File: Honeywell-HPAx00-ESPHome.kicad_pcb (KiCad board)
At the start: 2 copper layers, 215.9 x 50.8 mm, 25 parts, among them J1 Conn_01x06, J2 Conn_01x01, J3 Conn_01x01, J4 Conn_01x01, J5 Conn_01x01, J6 Conn_01x01, J7 Conn_01x01, U1 mini_esp32

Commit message: Update design
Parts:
- moved C1 47.9 mm to (187.0, 102.7)
- moved C2 47.9 mm to (152.0, 101.0)
- moved C3 47.9 mm to (108.4, 80.7)
- moved C4 47.9 mm to (142.2, 106.2)
- moved C5 47.9 mm to (65.2, 88.2)
- moved C6 47.9 mm to (203.7, 83.7)
- moved D1 47.9 mm to (145.2, 103.7)
- moved D10 47.9 mm to (199.2, 78.7)
- moved D11 47.9 mm to (229.7, 88.7)
- moved D2 47.9 mm to (137.5, 105.6)
- moved D3 47.9 mm to (90.2, 80.7)
- moved D4 47.9 mm to (90.2, 96.2)
- moved D5 47.9 mm to (59.7, 98.7)
- moved D7 47.9 mm to (59.7, 78.7)
- moved D8 47.9 mm to (199.2, 98.7)
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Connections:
- U1 pad 13: unconnected-(U1-IO_14/TMS-Pad13) -> BUTT_PREFILTER
- U1 pad 26: /FAN_W -> /FAN_L
- U1 pad 27: /FAN_H -> /FAN_W
- U1 pad 28: /FAN_L -> BUTT_FILTER
- U1 pad 29: unconnected-(U1-IO_17/D3-Pad29) -> /FAN_H
- U1 pad 30: unconnected-(U1-IO_12/TDI-Pad30) -> BUTT_TIMER
- U1 pad 32: BUTT_TIMER -> unconnected-(U1-IO_04-Pad32)
- U1 pad 34: BUTT_PREFILTER -> unconnected-(U1-IO_00-Pad34)
- U1 pad 36: BUTT_FILTER -> Net-(D2-DIN)
- U1 pad 6: Net-(D2-DIN) -> unconnected-(U1-IO_26/D0-Pad6)
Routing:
- net Net-(D2-DIN): track 58.9 -> 25.2 mm
- net BUTT_PREFILTER: track 87.2 -> 114.1 mm, vias 2 -> 0
- net BUTT_TIMER: track 126.9 -> 142.8 mm, vias 4 -> 0
- net Net-(D2-DOUT): track 72.6 -> 86.5 mm, vias 0 -> 2
- net /FAN_H: track 74.6 -> 82.6 mm
- net /FAN_W: track 58.9 -> 63.8 mm, vias 1 -> 2
- net BUTT_FILTER: track 101.0 -> 97.2 mm, vias 2 -> 0
- net Net-(D4-DOUT): track 44.2 -> 40.4 mm, vias 0 -> 2
- net /FAN_M: track 67.3 -> 69.1 mm
- net GND: track 170.3 -> 168.5 mm
- net Net-(D7-DOUT): track 187.5 -> 189.0 mm, vias 2 -> 4
- net BUTT_DIMMER: track 73.8 -> 74.3 mm, vias 2 -> 0
- net /FAN_L: track 63.1 -> 62.8 mm, vias 2 -> 1
- net +5V: track 284.3 -> 284.1 mm, vias 5 -> 7
- net BUTT_TURBO: track 42.5 -> 42.6 mm, vias 2 -> 0

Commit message: final tweaks
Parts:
- J2, J3, J4, J5, J6, J7: footprint TestPoint:TestPoint_THTPad_D1.5mm_Drill0.7mm -> TestPoint:TestPoint_THTPad_D2.0mm_Drill1.0mm

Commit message: Fix issues from production
1. clear space around buttons on ground plane
2. increase capacitor to 4.7mF (1mF would be an absolute minimum)
3. increase hole size for connector, since it's a very tight fit
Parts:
- C3: value 470u -> 4700u; footprint Capacitor_THT:CP_Radial_D8.0mm_P3.50mm -> Capacitor_THT:CP_Radial_D12.5mm_P5.00mm
- moved C3 2.42 mm to (110.0, 82.5)
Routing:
- net GND: track 168.5 -> 173.0 mm
- net +5V: track 284.1 -> 284.6 mm

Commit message: Update with complete instructions
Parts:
- C3: value 4700u -> 1000uF; footprint Capacitor_THT:CP_Radial_D12.5mm_P5.00mm -> Capacitor_THT:CP_Radial_D8.0mm_P3.50mm
- moved C3 4.16 mm to (106.0, 81.3), turned to -90 degrees
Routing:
- net GND: track 173.0 -> 95.9 mm
- net BUTT_FILTER: track 97.2 -> 107.8 mm
- net +5V: track 284.6 -> 285.5 mm

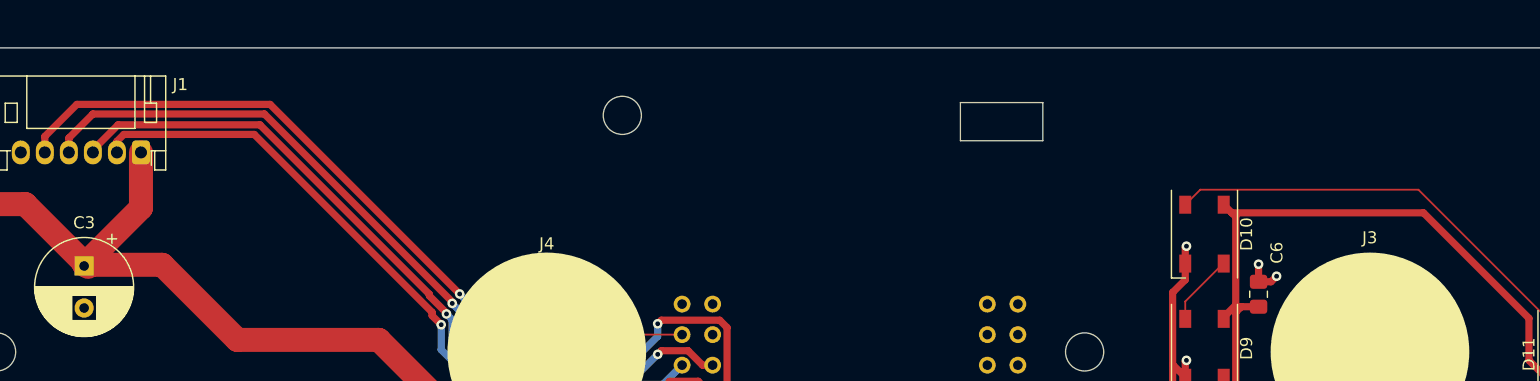
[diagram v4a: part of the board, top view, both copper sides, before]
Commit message: Add connector for extra 5V PSU
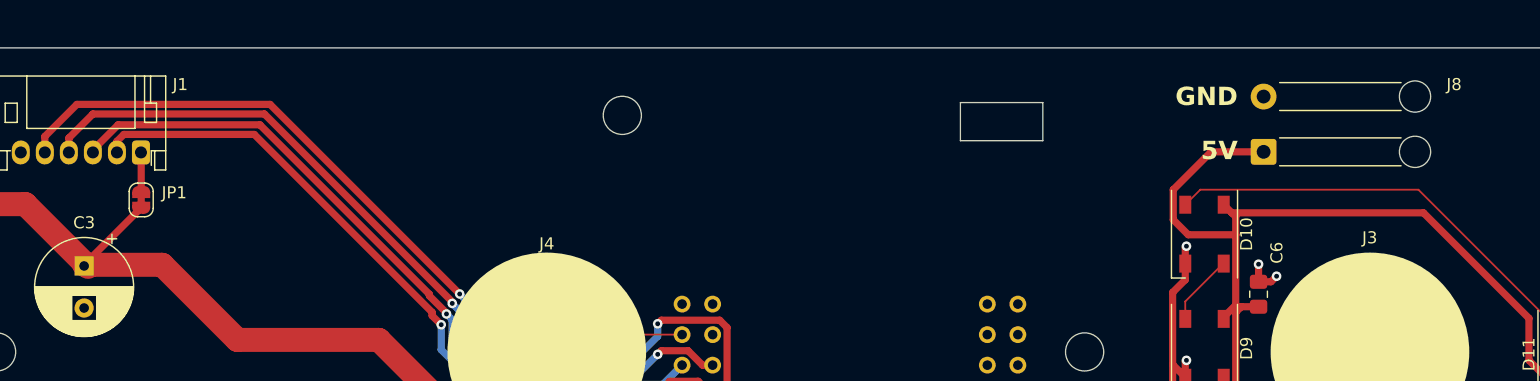
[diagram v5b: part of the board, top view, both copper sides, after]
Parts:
- added J8: Conn_01x02, Connector_Wire:SolderWire-0.5sqmm_1x02_P4.6mm_D0.9mm_OD2.1mm_Relief, F.Cu at (204.2, 71.8)
- added JP1: Jumper_2_Bridged, Jumper:SolderJumper-2_P1.3mm_Bridged_RoundedPad1.0x1.5mm, F.Cu at (110.8, 75.8)
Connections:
- J1 pad 1: +5V -> Net-(J1-Pin_1)
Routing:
- net +5V: track 285.5 -> 298.1 mm
- net Net-(J1-Pin_1): track 0.00 -> 3.20 mm
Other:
- board text added: "5V"
- board text added: "GND"

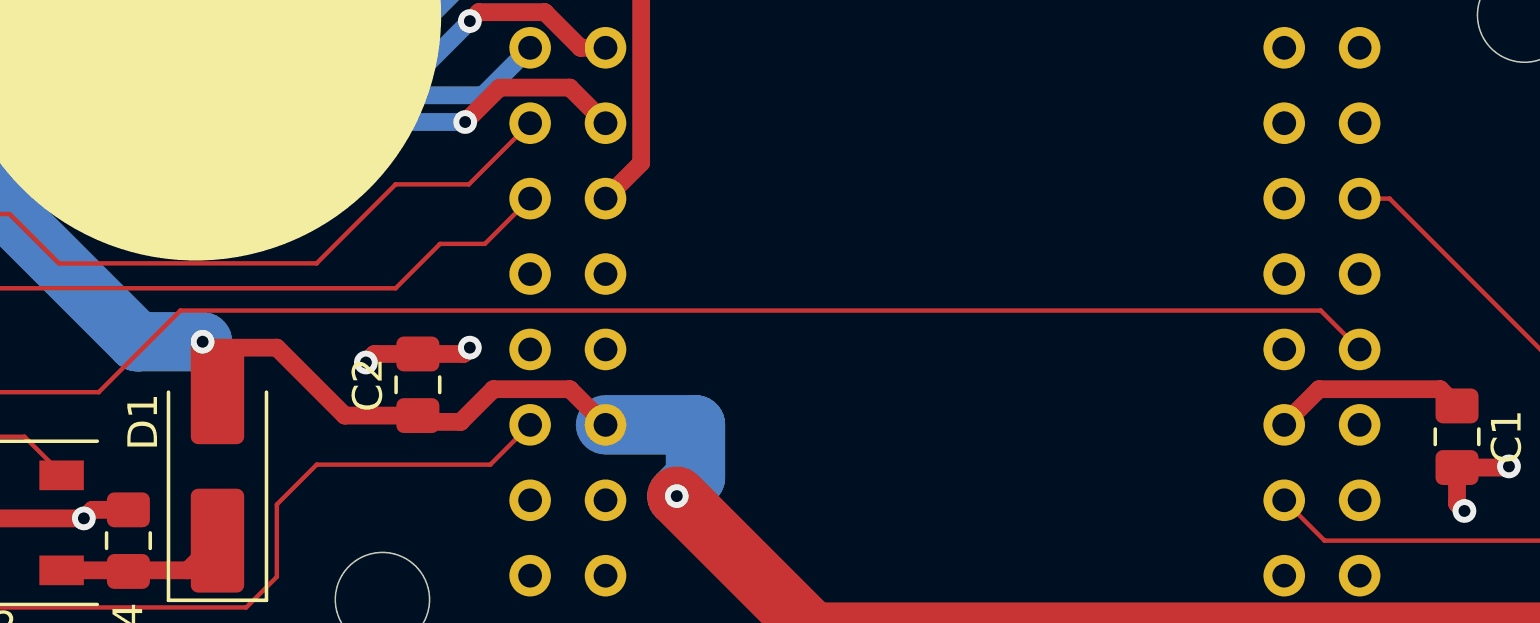
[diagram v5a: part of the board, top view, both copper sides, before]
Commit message: Move prefilter to GPIO4 (#1)
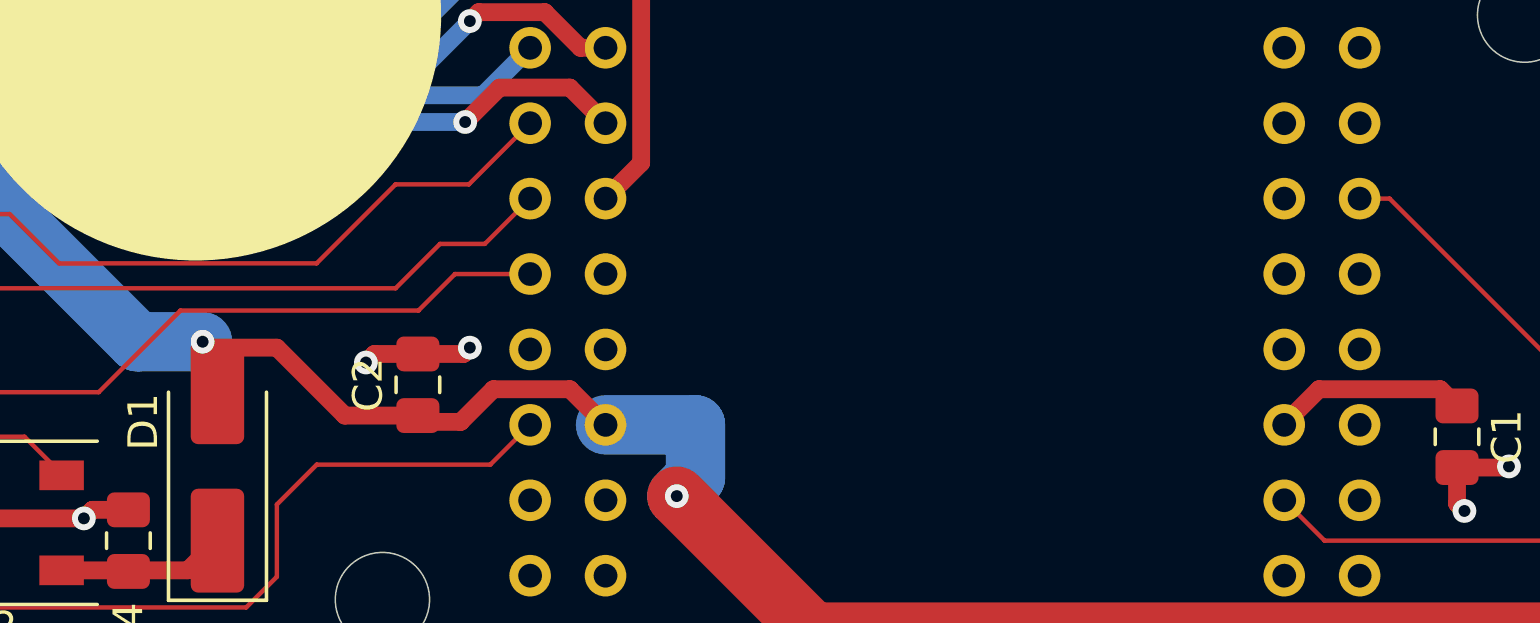
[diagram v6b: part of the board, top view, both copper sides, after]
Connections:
- U1 pad 13: BUTT_PREFILTER -> unconnected-(U1-IO_14/TMS-Pad13)
- U1 pad 32: unconnected-(U1-IO_04-Pad32) -> BUTT_PREFILTER
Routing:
- net BUTT_PREFILTER: track 114.1 -> 86.1 mm
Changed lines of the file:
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@@
 	(net 45 "/4.3V")
 	(net 46 "unconnected-(U1-IO_23{slash}D7-Pad12)")
-	(net 47 "unconnected-(U1-IO_04-Pad32)")
+	(net 47 "unconnected-(U1-IO_14{slash}TMS-Pad13)")
 	(net 48 "unconnected-(U1-IO_00-Pad34)")
 	(net 49 "unconnected-(U1-IO_26{slash}D0-Pad6)")
@@
 			(layers "*.Cu" "*.Mask")
 			(remove_unused_layers no)
-			(net 12 "BUTT_PREFILTER")
+			(net 47 "unconnected-(U1-IO_14{slash}TMS-Pad13)")
 			(pinfunction "IO_14/TMS")
-			(pintype "bidirectional")
+			(pintype "bidirectional+no_connect")
 		)
 		(pad "14" thru_hole circle
@@
 			(layers "*.Cu" "*.Mask")
 			(remove_unused_layers no)
-			(net 47 "unconnected-(U1-IO_04-Pad32)")
+			(net 12 "BUTT_PREFILTER")
 			(pinfunction "IO_04")
-			(pintype "bidirectional+no_connect")
+			(pintype "bidirectional")
 		)
 		(pad "33" thru_hole circle
@@
 	)
 	(segment
-		(start 183.7005 99.7606)
-		(end 182.3905 98.4506)
+		(start 143.9805 98.4506)
+		(end 152 98.4506)
 		(width 0.15)
 		(layer "F.Cu")
@@
 	)
 	(segment
-		(start 143.9805 98.4506)
-		(end 182.3905 98.4506)
+		(start 127.7305 103.7006)
+		(end 130.2305 101.2006)
 		(width 0.15)
 		(layer "F.Cu")
@@
 	)
 	(segment
-		(start 127.7305 103.7006)
-		(end 130.2305 101.2006)
+		(start 155.7605 97.2206)
+		(end 153.23 97.2206)
 		(width 0.15)
 		(layer "F.Cu")
@@
 		(width 0.15)
 		(layer "F.Cu")
+		(net 12)
+	)
+	(segment
+		(start 153.23 97.2206)
+		(end 152 98.4506)
+		(width 0.15)
+		(layer "F.Cu")

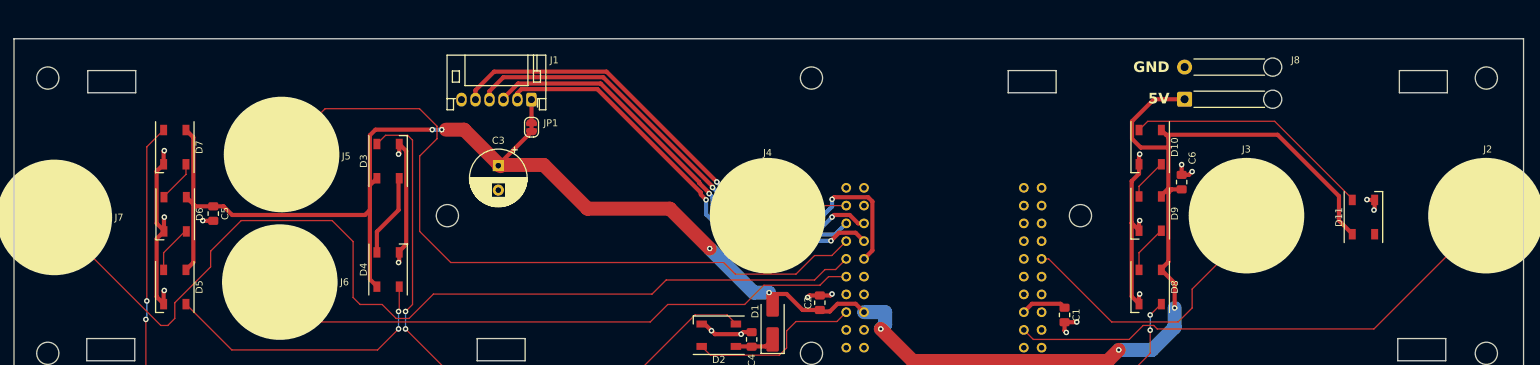
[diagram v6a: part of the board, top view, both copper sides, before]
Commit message: Updated PCB with new spring footprints
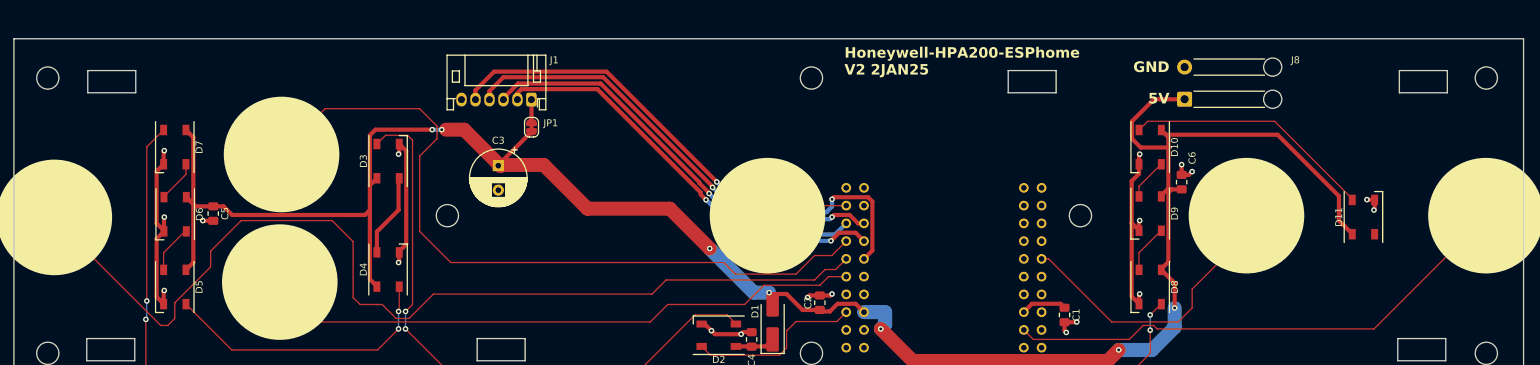
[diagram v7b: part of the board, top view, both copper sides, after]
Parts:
- J2, J3, J4, J5, J6, J7: footprint TestPoint:TestPoint_THTPad_D2.0mm_Drill1.0mm -> TestPoint:Honeywell V1+2 Spring
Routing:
- net BUTT_TURBO: track 42.6 -> 52.4 mm
- net BUTT_PREFILTER: track 86.1 -> 95.9 mm
- net BUTT_DIMMER: track 74.3 -> 84.1 mm
- net BUTT_TIMER: track 142.8 -> 152.6 mm
- net BUTT_FILTER: track 107.8 -> 117.6 mm
- net BUTT_POWER: track 11.5 -> 21.1 mm
- net /FAN_H: track 82.6 -> 77.8 mm
- net /FAN_M: track 69.1 -> 64.6 mm
- net /FAN_L: track 62.8 -> 59.6 mm
- net /FAN_W: track 63.8 -> 60.9 mm
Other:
- board text added: "Honeywell-HPA200-ESPhome V2 2JAN25"
